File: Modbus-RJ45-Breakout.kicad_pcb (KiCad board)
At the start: 2 copper layers, 87 x 68 mm, 140 parts, among them J1 RJ45_Weidmueller_2562920000, J2 RJ45_Weidmueller_2562920000, J3 Conn_01x04, J4 Conn_01x04, J5 USB_B_Mini, J6 2X04, Q1 BSP250, U1 FT2232D, U2 WE-TVS-82400102, U3 MAX485E, U4 ADM2687E, U5 93LC46B, U6 WE-TVS-82400102, U7 MAX485E, U8 ADM2687E, Y1 6MHz

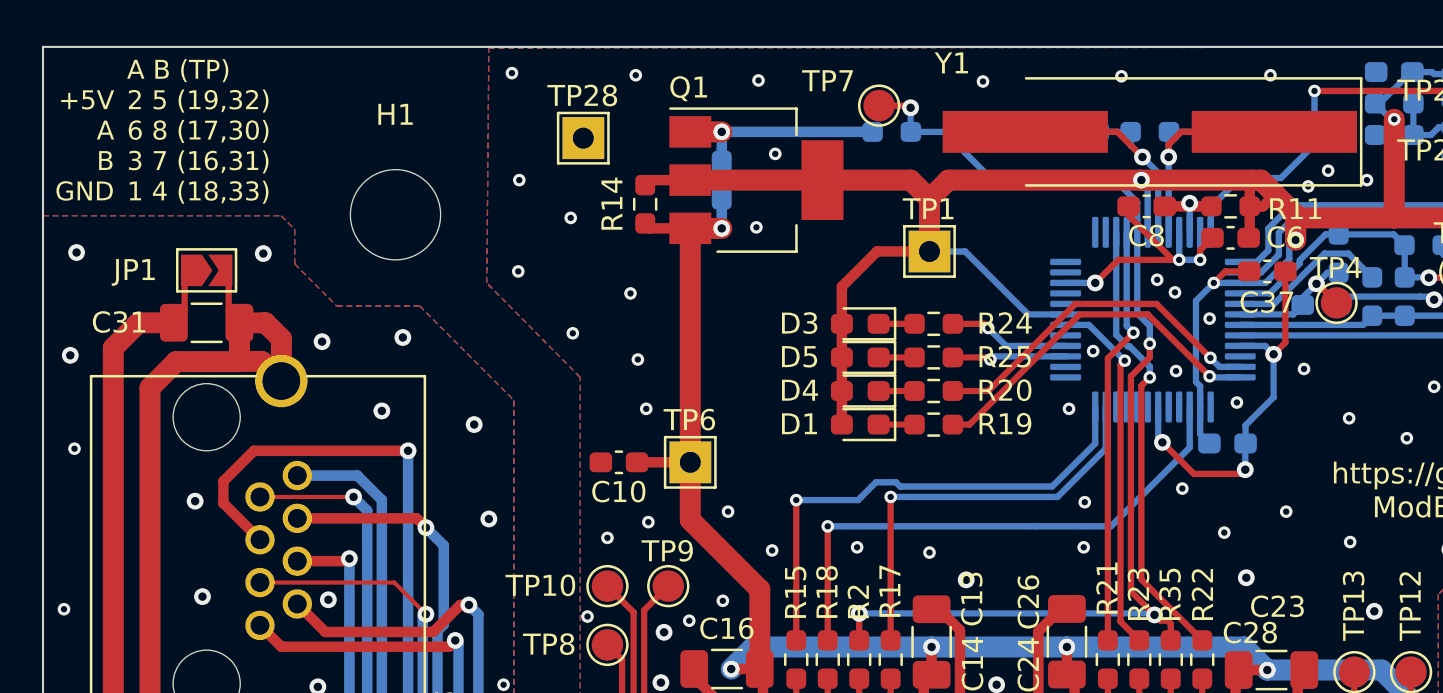
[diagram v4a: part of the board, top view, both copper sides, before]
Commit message: Moved the terminal docs to the middle of the PCB
...to be able to read it through the cut out of the case.
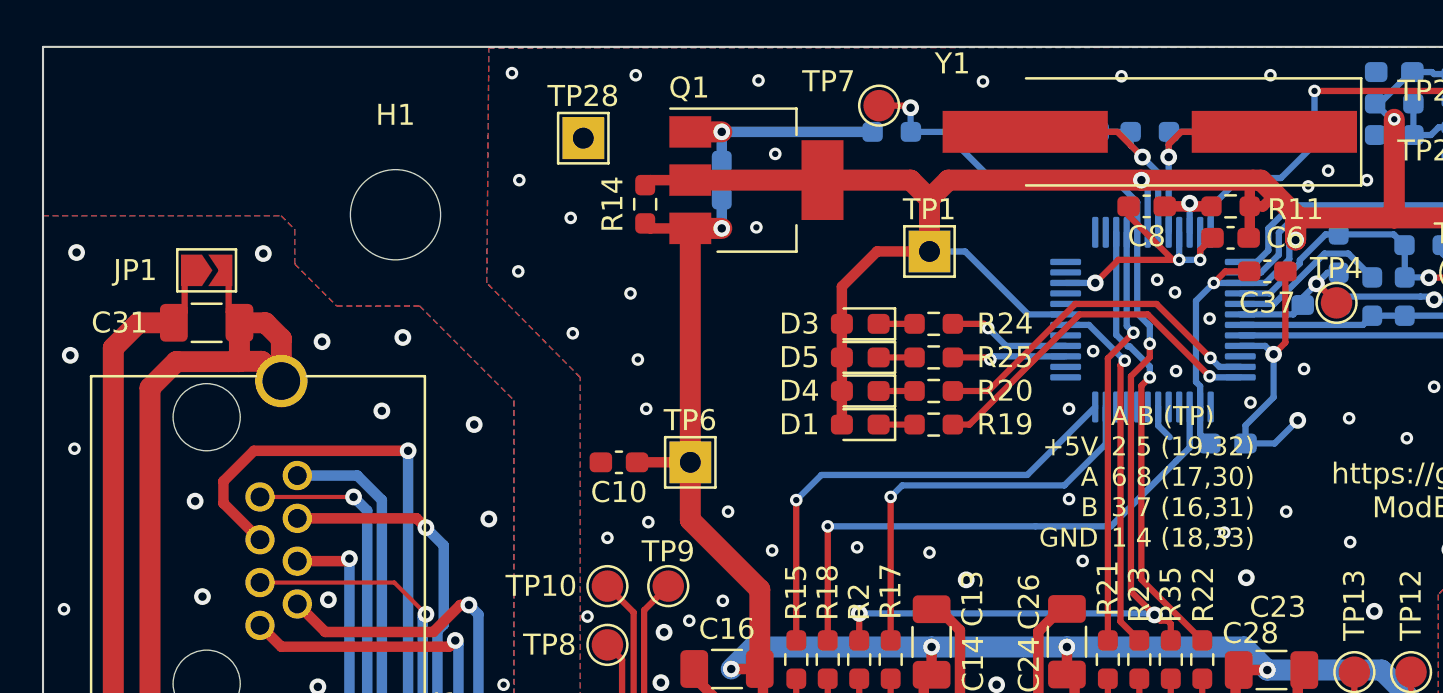
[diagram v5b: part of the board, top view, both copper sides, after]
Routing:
- net GND: track 141.1 -> 138.0 mm, vias 105 -> 103
- net Net-(R15-Pad1): track 24.0 -> 22.8 mm

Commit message: Fixed all issues and added Gerber exports
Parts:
- added DRA1: APRA 449-440-45, the78mole:Dummy_0, F.Cu at (129.7, 121.1)
- added J7: WAGO 2734-104, the78mole:Dummy_0, F.Cu at (129.7, 128.7)
- added J8: WAGO 2734-104, the78mole:Dummy_0, F.Cu at (129.7, 125.2)
- added R36: 27, Resistor_SMD:R_0603_1608Metric_Pad0.98x0.95mm_HandSolder, F.Cu at (88.2, 80.1)
- added R37: 27, Resistor_SMD:R_0603_1608Metric_Pad0.98x0.95mm_HandSolder, F.Cu at (103.0, 80.1)
- J3: value Conn_01x04 -> Bus_2
- J4: value Conn_01x04 -> BUS_1
- R2, R35: value 27 -> np
- R29, R3: value 560 -> 1K
- R8: value 0 -> np
- R9: value np -> 1K5
- moved R18 1.85 mm to (87.4, 77.3)
- moved R2 1.85 mm to (88.9, 77.3)
- moved R35 1.55 mm to (103.8, 77.7)
- moved R23 1.55 mm to (102.2, 77.7)
- moved C26 0.20 mm to (98.6, 78.3)
- moved R21 0.20 mm to (100.5, 79.2)
- moved R22 0.20 mm to (105.5, 79.2)
- moved C23 0.15 mm to (108.7, 79.7)
- moved R15 0.15 mm to (85.8, 79.2)
- moved R17 0.15 mm to (90.5, 79.2)
- moved C13 0.10 mm to (92.5, 78.4)
- moved C16 0.10 mm to (82.5, 79.7)
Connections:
- U4 pad 11: /B_1 -> /A_1
- U4 pad 12: /A_1 -> /B_1
- U4 pad 13: /A_1 -> /B_1
- U4 pad 14: /B_1 -> /A_1
- U6 pad 1: /A_2 -> /B_2
- U6 pad 3: /B_2 -> /A_2
- U6 pad 4: /B_2 -> /A_2
- U6 pad 6: /A_2 -> /B_2
- U8 pad 11: /B_2 -> /A_2
- U8 pad 12: /A_2 -> /B_2
- U8 pad 13: /A_2 -> /B_2
- U8 pad 14: /B_2 -> /A_2
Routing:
- net /B_1: track 156.9 -> 152.9 mm
- net /A_1: track 152.5 -> 154.8 mm
- net /A_2: track 149.3 -> 151.4 mm
- net TXDEN1: track 24.5 -> 26.5 mm
- net Net-(R2-Pad1): track 16.3 -> 18.3 mm
- net /B_2: track 158.4 -> 156.4 mm
- net Net-(R18-Pad1): track 26.2 -> 24.3 mm
- net Net-(R35-Pad1): track 15.6 -> 17.2 mm
- net Net-(R23-Pad1): track 17.3 -> 15.8 mm
- net TXDEN2: track 20.7 -> 22.2 mm
